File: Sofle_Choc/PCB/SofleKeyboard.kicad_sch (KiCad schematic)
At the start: 110 parts, among them J2 4PIN, J3 OLED, P1 i2c_pin, P2 i2c_pin, SW1 SW_PUSH_LED, SW10 SW_PUSH_LED, SW11 SW_PUSH_LED, SW12 SW_PUSH_LED, SW13 SW_PUSH_LED, SW14 SW_PUSH_LED, SW15 SW_PUSH_LED, SW16 SW_PUSH_LED, SW17 SW_PUSH_LED, SW18 SW_PUSH_LED, SW19 SW_PUSH_LED, SW2 SW_PUSH_LED, SW20 SW_PUSH_LED, SW21 SW_PUSH_LED, SW22 SW_PUSH_LED, SW23 SW_PUSH_LED, SW24 SW_PUSH_LED, SW25 Rotary_Encoder_Switch, SW26 SW_PUSH_LED, SW27 SW_PUSH_LED, SW28 SW_PUSH_LED, SW29 SW_PUSH_LED, SW3 SW_PUSH_LED, SW30 SW_PUSH_LED, SW31 SW_PUSH_LED, SW32 SW_PUSH_LED, SW33 SW_PUSH_LED, SW4 SW_PUSH_LED, SW5 SW_PUSH_LED, SW6 SW_PUSH_LED, SW7 SW_PUSH_LED, SW8 SW_PUSH_LED, SW9 SW_PUSH_LED, U1 ProMicro

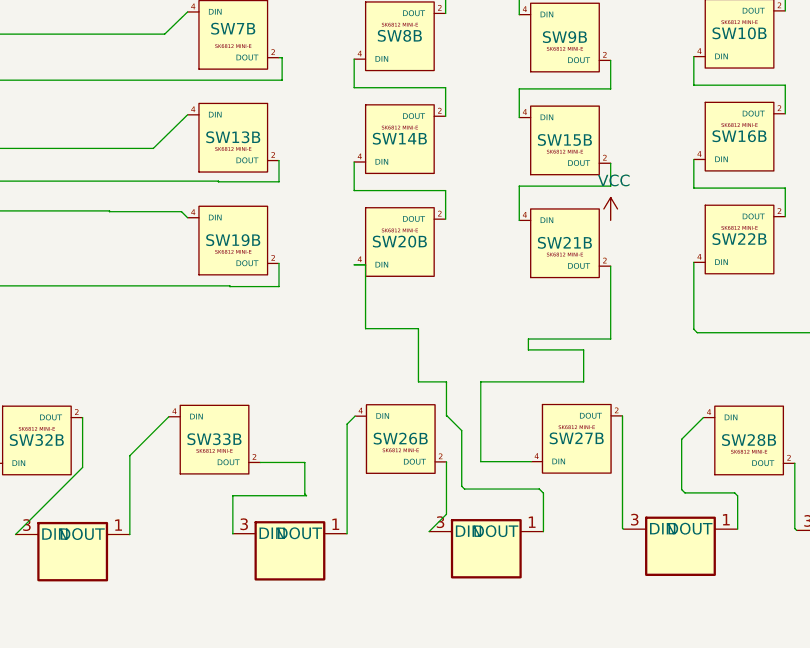
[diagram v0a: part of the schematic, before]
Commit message: Underglow added
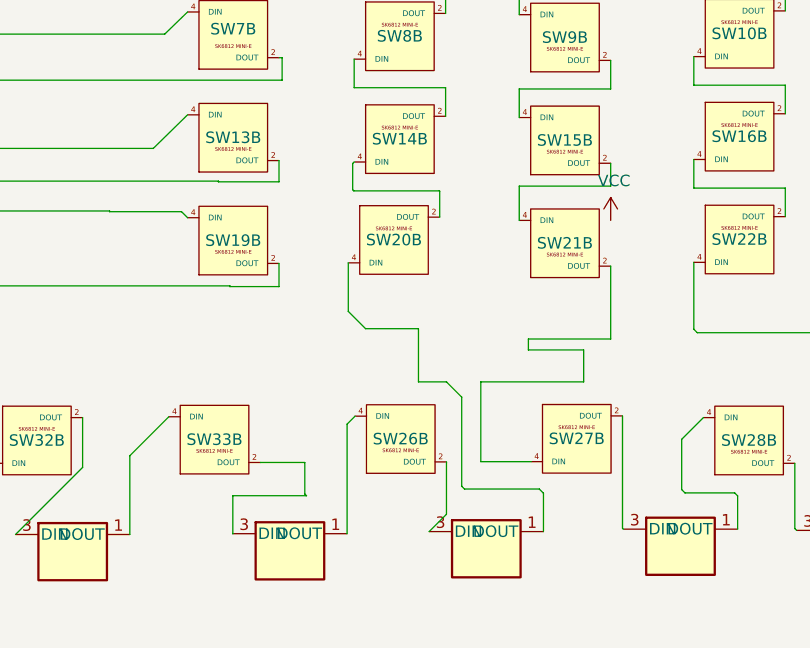
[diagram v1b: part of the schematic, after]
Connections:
- net VCC: no longer SW20.4 (DIN)
- net at D41.1 (DOUT): now also SW20.4 (DIN)
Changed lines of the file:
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@@
     (stroke (width 0) (type default))
   )
-  (wire (pts (xy 200.1417 84.3476) (xy 200.1417 88.1576))
-    (stroke (width 0) (type default))
-  )
   (wire (pts (xy 189.0978 89.0415) (xy 189.9817 88.1576))
     (stroke (width 0) (type default))
@@
     (stroke (width 0) (type default))
   )
+  (wire (pts (xy 189.7184 60.0826) (xy 189.8858 59.9152))
+    (stroke (width 0) (type default))
+  )
   (wire (pts (xy 208.2269 62.5947) (xy 208.2269 66.4047))
     (stroke (width 0) (type default))
@@
     (stroke (width 0) (type default))
   )
+  (wire (pts (xy 199.3481 63.1231) (xy 189.844 63.1231))
+    (stroke (width 0) (type default))
+  )
   (wire (pts (xy 232.1661 96.6861) (xy 226.6457 96.6861))
     (stroke (width 0) (type default))
@@
     (stroke (width 0) (type default))
   )
-  (wire (pts (xy 200.0458 63.0902) (xy 189.8858 63.0902))
-    (stroke (width 0) (type default))
-  )
   (wire (pts (xy 60.96 24.13) (xy 68.58 24.13))
     (stroke (width 0) (type default))
@@
     (stroke (width 0) (type default))
   )
-  (wire (pts (xy 201.835 89.7577) (xy 200.1417 88.0644))
-    (stroke (width 0) (type default))
-  )
   (wire (pts (xy 27.94 99.06) (xy 30.48 99.06))
     (stroke (width 0) (type default))
@@
     (stroke (width 0) (type default))
   )
+  (wire (pts (xy 199.39 66.04) (xy 199.39 63.165))
+    (stroke (width 0) (type default))
+  )
   (wire (pts (xy 269.2148 51.381) (xy 269.2148 48.206))
     (stroke (width 0) (type default))
@@
     (stroke (width 0) (type default))
   )
+  (wire (pts (xy 189.844 63.1231) (xy 189.7184 62.9975))
+    (stroke (width 0) (type default))
+  )
   (wire (pts (xy 238.8465 93.3958) (xy 238.8465 100.642))
     (stroke (width 0) (type default))
@@
     (stroke (width 0) (type default))
   )
+  (wire (pts (xy 199.39 63.165) (xy 199.3481 63.1231))
+    (stroke (width 0) (type default))
+  )
   (wire (pts (xy 167.5631 58.4061) (xy 171.3731 54.6757))
     (stroke (width 0) (type default))
@@
     (stroke (width 0) (type default))
   )
+  (wire (pts (xy 201.835 86.0409) (xy 200.1417 84.3476))
+    (stroke (width 0) (type default))
+  )
   (wire (pts (xy 227.6258 78.4999) (xy 228.0102 78.8843))
     (stroke (width 0) (type default))
@@
     (stroke (width 0) (type default))
   )
-  (wire (pts (xy 200.0458 66.2652) (xy 200.0458 63.0902))
-    (stroke (width 0) (type default))
-  )
   (wire (pts (xy 29.21 96.52) (xy 29.21 107.95))
     (stroke (width 0) (type default))
   )
-  (wire (pts (xy 191.1494 71.3452) (xy 189.8858 71.3452))
-    (stroke (width 0) (type default))
-  )
   (wire (pts (xy 200.0458 40.2302) (xy 189.8858 40.2302))
     (stroke (width 0) (type default))
   )
-  (wire (pts (xy 191.1494 78.4345) (xy 191.1494 71.3452))
-    (stroke (width 0) (type default))
-  )
   (wire (pts (xy 298.8449 57.1439) (xy 284.9115 57.1439))
     (stroke (width 0) (type default))
@@
     (stroke (width 0) (type default))
   )
-  (wire (pts (xy 201.835 95.9418) (xy 201.835 89.7577))
-    (stroke (width 0) (type default))
-  )
   (wire (pts (xy 203.9517 93.2097) (xy 209.5388 93.2097))
     (stroke (width 0) (type default))
@@
     (stroke (width 0) (type default))
   )
-  (wire (pts (xy 189.8858 63.0902) (xy 189.8858 59.9152))
-    (stroke (width 0) (type default))
-  )
   (wire (pts (xy 222.6295 223.2846) (xy 242.9495 223.2846))
     (stroke (width 0) (type default))
@@
     (stroke (width 0) (type default))
   )
+  (wire (pts (xy 201.835 95.9418) (xy 201.835 86.0409))
+    (stroke (width 0) (type default))
+  )
   (wire (pts (xy 181.5331 36.8957) (xy 181.5331 39.4357))
     (stroke (width 0) (type default))
@@
     (stroke (width 0) (type default))
   )
+  (wire (pts (xy 189.7184 62.9975) (xy 189.7184 60.0826))
+    (stroke (width 0) (type default))
+  )
   (wire (pts (xy 218.3869 40.3697) (xy 208.2269 40.3697))
     (stroke (width 0) (type default))
@@
     (stroke (width 0) (type default))
   )
+  (wire (pts (xy 189.23 76.5151) (xy 191.1494 78.4345))
+    (stroke (width 0) (type default))
+  )
   (wire (pts (xy 240.8282 27.5819) (xy 240.695 27.4948))
     (stroke (width 0) (type default))
@@
     (stroke (width 0) (type default))
   )
+  (wire (pts (xy 189.23 71.12) (xy 189.23 76.5151))
+    (stroke (width 0) (type default))
+  )
   (wire (pts (xy 29.21 107.95) (xy 30.48 107.95))
     (stroke (width 0) (type default))
@@
     )
   )
-  (symbol (lib_id "SofleKeyboard:SW_PUSH_LED") (at 194.9658 68.8052 180) (unit 2)
-    (in_bom yes) (on_board yes) (dnp no)
-    (property "Reference" "SW20" (at 194.9658 68.8052 0)
-      (effects (font (size 1.27 1.27)))
-    )
-    (property "Value" "SW_PUSH_LED" (at 194.9658 75.7648 0)
-      (effects (font (size 1.27 1.27)) hide)
-    )
-    (property "Footprint" "SofleChoc:Choc_Hotswap_SK6812MiniE" (at 194.9658 75.1552 0)
-      (effects (font (size 1.27 1.27)) hide)
-    )
-    (property "Datasheet" "" (at 194.9658 75.1552 0)
-      (effects (font (size 1.27 1.27)) hide)
-    )
-    (pin "3")
-    (pin "4")
-    (pin "1")
-    (pin "6")
-    (pin "2")
-    (pin "5")
-    (instances
-      (project "SofleKeyboard"
-        (path "/683c928e-de74-4e53-88df-31c998b95d51"
-          (reference "SW20") (unit 2)
-        )
-      )
-    )
-  )
   (symbol (lib_id "SofleKeyboard:SW_PUSH_LED") (at 176.4531 68.6457 0) (mirror y) (unit 2)
     (in_bom yes) (on_board yes) (dnp no)
@@
         )
       )
+    )
+  )
+  (symbol (lib_id "SofleKeyboard:SW_PUSH_LED") (at 194.31 68.58 180) (unit 2)
+    (in_bom yes) (on_board yes) (dnp no)
+    (property "Reference" "SW20" (at 194.31 68.58 0)
+      (effects (font (size 1.27 1.27)))
+    )
+    (property "Value" "SW_PUSH_LED" (at 194.31 75.5396 0)
+      (effects (font (size 1.27 1.27)) hide)
+    )
+    (property "Footprint" "SofleChoc:Choc_Hotswap_SK6812MiniE" (at 194.31 74.93 0)
+      (effects (font (size 1.27 1.27)) hide)
+    )
+    (property "Datasheet" "" (at 194.31 74.93 0)
+      (effects (font (size 1.27 1.27)) hide)
+    )
+    (pin "2")
+    (pin "1")
+    (pin "3")
+    (pin "4")
+    (pin "5")
+    (pin "6")
+    (instances
+      (project "SofleKeyboard"
+        (path "/683c928e-de74-4e53-88df-31c998b95d51"
+          (reference "SW20") (unit 2)
+        )
+      )

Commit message: Cleanup
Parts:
- J2: footprint SofleKeyboard-footprint:MJ-4PP-9 -> SofleChoc:3.5mm_6_contacts_4_conductors_audio_plug
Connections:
- net GND: now also J2.4; no longer J2.2
- net i2c_c: no longer names the net of P1.1 (Pin_1)
- net i2c_c: now also J2.2; no longer J2.4
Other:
- moved on the sheet: P1, P2, R1, R2, W1
